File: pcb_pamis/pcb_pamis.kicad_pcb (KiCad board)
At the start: 4 copper layers, 79 x 100.5 mm, 62 parts, among them J1 USB_C_Receptacle_USB2.0_16P, J10 Conn_01x03, J11 Conn_01x03, J12 Conn_02x06_Odd_Even, J2 1755736, J3 Conn_01x04, J4 Conn_01x04, J5 Conn_01x04, J6 Conn_01x05, J7 Conn_01x05, J8 Conn_01x05, J9 Conn_01x03, Q1 Q_NPN_BEC, Q2 Q_NPN_BEC, SW1 SW_Push, U1 ESP32-WROOM-32UE, U2 CP2102N-Axx-xQFN28, U3 TMC2209_SILENTSTEPSTICK, U4 TMC2209_SILENTSTEPSTICK, U5 TMC2209_SILENTSTEPSTICK

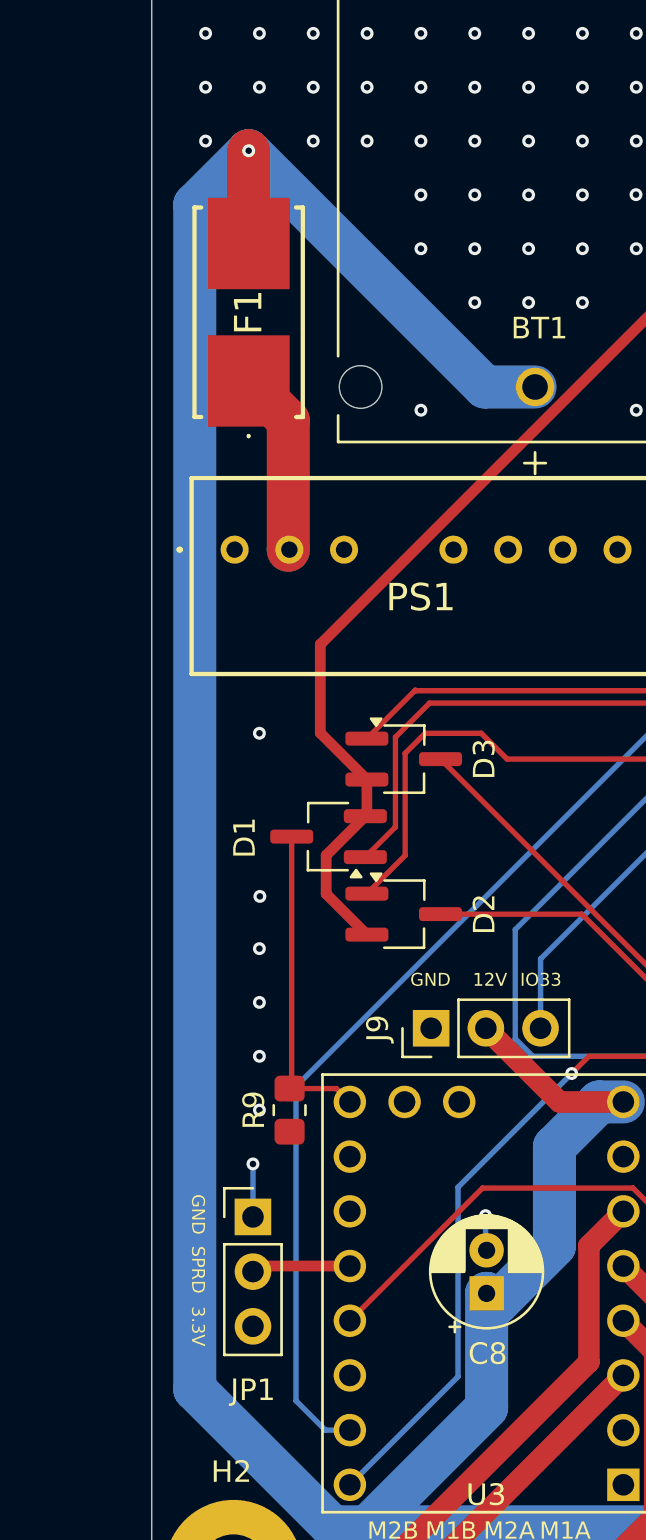
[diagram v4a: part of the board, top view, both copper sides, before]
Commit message: déplacement fusible
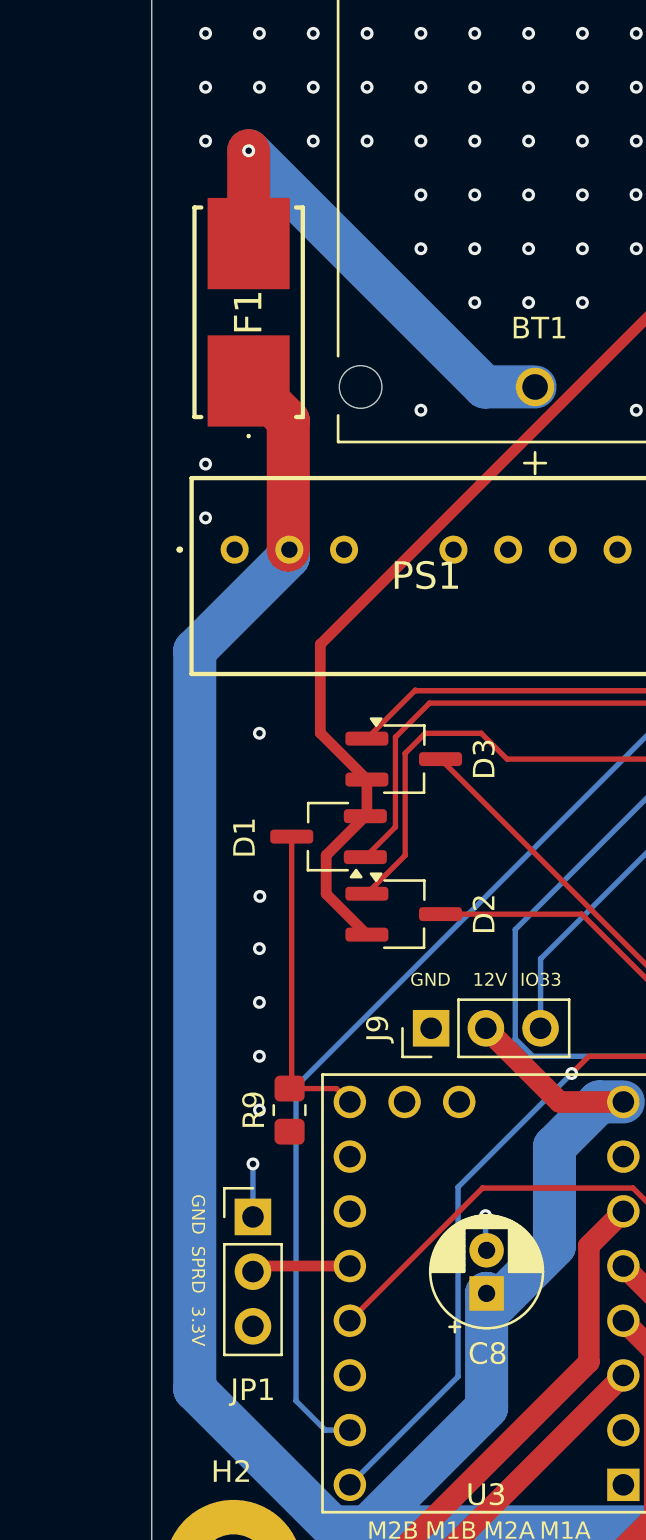
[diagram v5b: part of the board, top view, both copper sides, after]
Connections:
- BT1 pad P: VCC -> Net-(BT1-+)
- F1 pad 1: Net-(PS1-+VIN_(VCC)) -> VCC
- F1 pad 2: VCC -> Net-(BT1-+)
- PS1 pad 2: Net-(PS1-+VIN_(VCC)) -> VCC
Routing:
- net VCC: track 238.0 -> 206.8 mm, vias 1 -> 0
- net Net-(BT1-+): track 0.00 -> 22.2 mm, vias 0 -> 1
- net Net-(PS1-+VIN_(VCC)): track 8.70 -> 0.00 mm
- net GND: vias 460 -> 462
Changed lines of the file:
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@@
 	(net 101 "Net-(J1-CC2)")
 	(net 102 "unconnected-(J1-SBU2-PadB8)")
-	(net 103 "Net-(PS1-+VIN_(VCC))")
+	(net 103 "Net-(BT1-+)")
 	(footprint "Modelec:MODULE_TMC2209_SILENTSTEPSTICK"
 		(layer "F.Cu")
@@
 		(tags "Power Supply")
 		(property "Reference" "PS1"
-			(at 8.65 2.225 0)
+			(at 8.9 1.225 0)
 			(layer "F.SilkS")
 			(effects
@@
 		)
 		(fp_text user "${REFERENCE}"
-			(at 8.65 2.225 0)
+			(at 8.9 1.225 0)
 			(layer "F.Fab")
 			(effects
@@
 			(layers "*.Cu" "*.Mask")
 			(remove_unused_layers no)
-			(net 103 "Net-(PS1-+VIN_(VCC))")
+			(net 9 "VCC")
 			(pinfunction "+VIN_(VCC)")
 			(pintype "passive")
@@
 			(layers "*.Cu" "*.Mask")
 			(remove_unused_layers no)
-			(net 9 "VCC")
+			(net 103 "Net-(BT1-+)")
 			(pinfunction "+")
 			(pintype "passive")
@@
 			(size 3.81 4.24)
 			(layers "F.Cu" "F.Mask" "F.Paste")
-			(net 103 "Net-(PS1-+VIN_(VCC))")
+			(net 9 "VCC")
 			(pintype "passive")
 		)
@@
 			(size 3.81 4.24)
 			(layers "F.Cu" "F.Mask" "F.Paste")
-			(net 9 "VCC")
+			(net 103 "Net-(BT1-+)")
 			(pintype "passive")
 		)
@@
 	)
 	(via
+		(at 72 75.8)
+		(size 0.6)
+		(drill 0.3)
+		(layers "F.Cu" "B.Cu")
+		(free yes)
+		(net 5)
+	)
+	(via
 		(at 139.460805 35.840293)
 		(size 0.6)
@@
 	)
 	(via
+		(at 72 73.3)
+		(size 0.6)
+		(drill 0.3)
+		(layers "F.Cu" "B.Cu")
+		(free yes)
+		(net 5)
+	)
+	(via
 		(at 134.5 70.8)
 		(size 0.6)
@@
 	)
 	(segment
+		(start 75.84 71.28)
+		(end 75.84 77.3)
+		(width 2)
+		(layer "F.Cu")
+		(net 9)
+	)
+	(segment
 		(start 108.015 99.5)
 		(end 111.435 102.92)
@@
 	)
 	(segment
+		(start 74 69.44)
+		(end 75.84 71.28)
+		(width 2)
+		(layer "F.Cu")
+		(net 9)
+	)
+	(segment
 		(start 85.015 99.5)
 		(end 88.435 102.92)
@@
 	)
 	(segment
-		(start 74 58.75)
-		(end 74 63.06)
+		(start 75.84 77.622)
+		(end 71.4975 81.9645)
 		(width 2)
-		(layer "F.Cu")
-		(net 9)
-	)
-	(via
-		(at 74 58.75)
-		(size 0.6)
-		(drill 0.3)
-		(layers "F.Cu" "B.Cu")
+		(layer "B.Cu")
 		(net 9)
 	)
@@
 	)
 	(segment
+		(start 71.4975 116.262288)
+		(end 77.890212 122.655)
+		(width 2)
+		(layer "B.Cu")
+		(net 9)
+	)
+	(segment
 		(start 131.6 111.8)
 		(end 133 110.4)
@@
 	)
 	(segment
-		(start 87.3 69.72)
-		(end 84.97 69.72)
-		(width 2)
-		(layer "B.Cu")
-		(net 9)
-	)
-	(segment
-		(start 74 58.75)
-		(end 71.4975 61.2525)
+		(start 71.4975 81.9645)
+		(end 71.4975 116.262288)
 		(width 2)
 		(layer "B.Cu")
@@
 	)
 	(segment
-		(start 71.4975 116.262288)
-		(end 77.890212 122.655)
-		(width 2)
-		(layer "B.Cu")
-		(net 9)
-	)
-	(segment
 		(start 85.05 111.81)
 		(end 85.510212 112.270212)
@@
 	)
 	(segment
-		(start 71.4975 61.2525)
-		(end 71.4975 116.262288)
-		(width 2)
-		(layer "B.Cu")
-		(net 9)
-	)
-	(segment
-		(start 84.97 69.72)
-		(end 74 58.75)
+		(start 77.890212 122.655)
+		(end 79.509788 122.655)
 		(width 2)
 		(layer "B.Cu")
@@
 	)
 	(segment
-		(start 77.890212 122.655)
-		(end 79.509788 122.655)
+		(start 75.84 77.220169)
+		(end 75.84 77.622)
 		(width 2)
 		(layer "B.Cu")
@@
 	)
 	(segment
-		(start 75.84 71.28)
-		(end 75.84 77.3)
+		(start 74 58.75)
+		(end 74 63.06)
 		(width 2)
 		(layer "F.Cu")
 		(net 103)
 	)
+	(via
+		(at 74 58.75)
+		(size 0.6)
+		(drill 0.3)
+		(layers "F.Cu" "B.Cu")
+		(net 103)
+	)
 	(segment
-		(start 74 69.44)
-		(end 75.84 71.28)
+		(start 87.3 69.72)
+		(end 84.97 69.72)
 		(width 2)
-		(layer "F.Cu")
+		(layer "B.Cu")
 		(net 103)
 	)
 	(segment
-		(start 75.84 77.220169)
-		(end 75.84 77.3)
+		(start 84.97 69.72)
+		(end 74 58.75)
 		(width 2)
 		(layer "B.Cu")

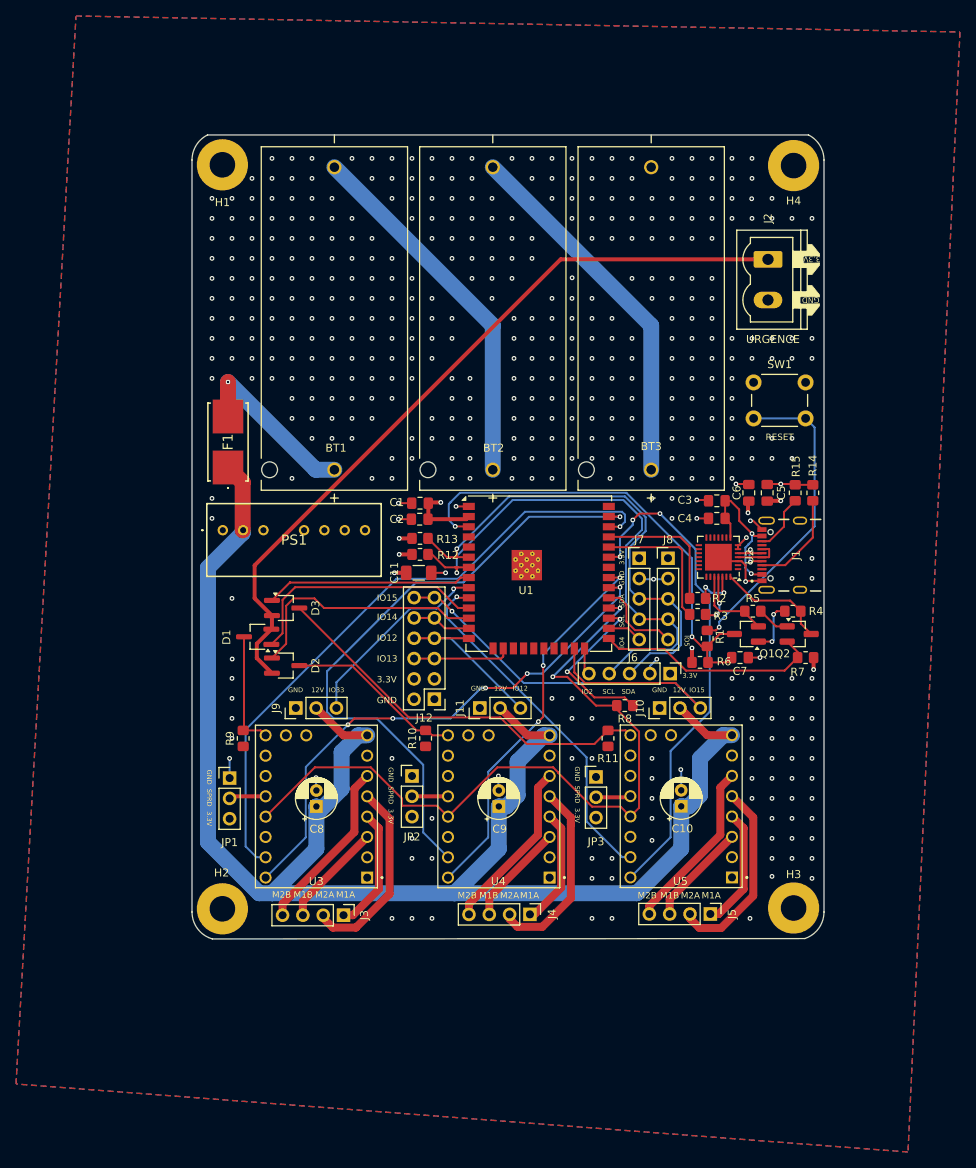
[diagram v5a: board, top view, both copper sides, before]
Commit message: Ajout empreinte condo couché + réparation contour PCB avec 7mm autour des trous de fixation
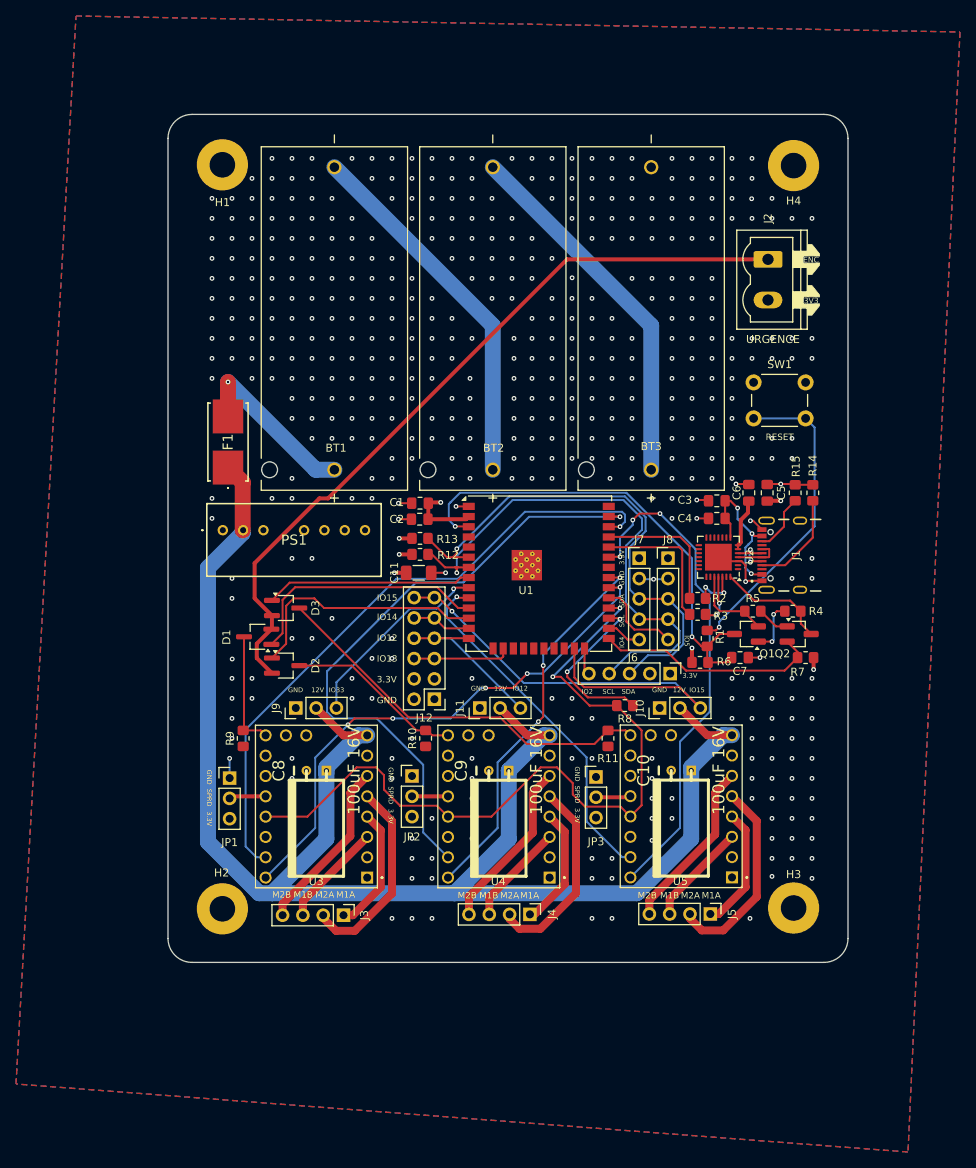
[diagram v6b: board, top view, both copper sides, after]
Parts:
- C10, C8, C9: footprint Capacitor_THT:CP_Radial_D5.0mm_P2.00mm -> w_capacitors:CP_6.3x11mm_horiz-L
- moved C10 4.48 mm to (130.7, 107.3)
- moved C8 4.48 mm to (85.0, 107.3)
- moved C9 4.48 mm to (107.8, 107.3)
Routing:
- net +3.3V: track 36.6 -> 25.5 mm, vias 9 -> 7
- net GND: track 42.7 -> 34.5 mm, vias 462 -> 498
- net TX_MOTEUR: track 94.5 -> 96.4 mm
- net VCC: track 206.8 -> 205.1 mm
- net Net-(J5-Pin_2): track 24.2 -> 25.1 mm
- net Net-(J4-Pin_2): track 24.0 -> 24.7 mm
- net Net-(J3-Pin_2): track 24.3 -> 25.0 mm
- net VBUS: vias 2 -> 3
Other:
- board size 79 x 100.5 mm -> 85 x 106 mm
